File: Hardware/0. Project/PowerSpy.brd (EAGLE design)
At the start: 55 x 70.5 mm, 87 parts, among them CN1 Mini-Fit 4T, IC1 CP2102N-A01-GQFN28, T1 SS8050, T2 SS8050, U1 MCP6021, U2 MCP6024, U3 ADS1115IDGST, U4 HLK-PM01, U5 NCP1117ST33T3G, U6 ESP32-WROOM-32D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

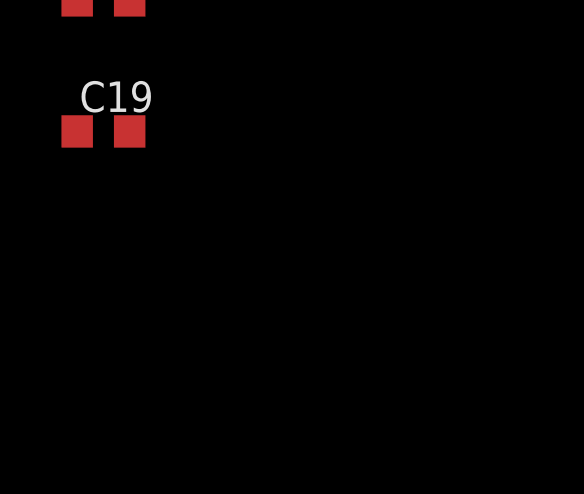
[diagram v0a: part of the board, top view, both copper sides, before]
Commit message: Pull-down resistor added to current AFE
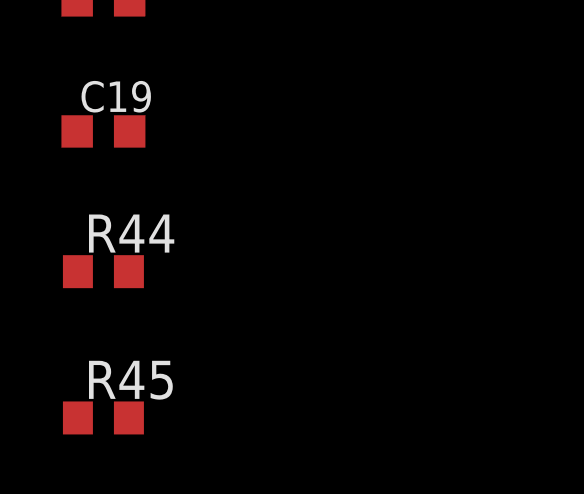
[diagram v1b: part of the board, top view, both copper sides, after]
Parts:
- added R44, R45: 1M (5%), rcl:R0603
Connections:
- net GND: now also R44.2, R45.2
- net N$35: now also R44.1
- net N$36: now also R45.1
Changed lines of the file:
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@@
 <attribute name="VALUE" x="-35.344" y="-184.1236" size="1.016" layer="27"/>
+</element>
+<element name="R44" library="rcl" library_urn="urn:adsk.eagle:library:334" package="R0603" package3d_urn="urn:adsk.eagle:package:23555/3" value="1M (5%)" x="-34.544" y="-187.1472" smashed="yes">
+<attribute name="NAME" x="-35.179" y="-186.5122" size="1.27" layer="25"/>
+<attribute name="POPULARITY" value="70" x="-34.544" y="-187.1472" size="1.778" layer="27" display="off"/>
+<attribute name="SPICEPREFIX" value="R" x="-34.544" y="-187.1472" size="1.778" layer="27" display="off"/>
+<attribute name="VALUE" x="-35.179" y="-189.0522" size="1.27" layer="27"/>
+</element>
+<element name="R45" library="rcl" library_urn="urn:adsk.eagle:library:334" package="R0603" package3d_urn="urn:adsk.eagle:package:23555/3" value="1M (5%)" x="-34.544" y="-192.024" smashed="yes">
+<attribute name="NAME" x="-35.179" y="-191.389" size="1.27" layer="25"/>
+<attribute name="POPULARITY" value="70" x="-34.544" y="-192.024" size="1.778" layer="27" display="off"/>
+<attribute name="SPICEPREFIX" value="R" x="-34.544" y="-192.024" size="1.778" layer="27" display="off"/>
+<attribute name="VALUE" x="-35.179" y="-193.929" size="1.27" layer="27"/>
 </element>
 </elements>
@@
 <contactref element="C3" pad="2"/>
 <contactref element="C19" pad="2"/>
+<contactref element="R44" pad="2"/>
+<contactref element="R45" pad="2"/>
+<wire x1="-33.694" y1="-187.1472" x2="-33.694" y2="-192.024" width="0" layer="19" extent="1-1"/>
+<wire x1="-33.669" y1="-182.4736" x2="-33.694" y2="-187.1472" width="0" layer="19" extent="1-1"/>
 <wire x1="-33.669" y1="-178.1048" x2="-33.669" y2="-182.4736" width="0" layer="19" extent="1-1"/>
 <wire x1="-35.3314" y1="-174.1424" x2="-33.669" y2="-178.1048" width="0" layer="19" extent="1-1"/>
@@
 <contactref element="U2" pad="10"/>
 <contactref element="X2" pad="1"/>
+<contactref element="R44" pad="1"/>
+<wire x1="-25.0786" y1="-115.062" x2="-35.394" y2="-187.1472" width="0" layer="19" extent="1-1"/>
 <wire x1="14" y1="10.345" x2="-25.0786" y2="-115.062" width="0" layer="19" extent="1-1"/>
 </signal>
@@
 <contactref element="X3" pad="1"/>
 <contactref element="U2" pad="12"/>
+<contactref element="R45" pad="1"/>
+<wire x1="-25.0786" y1="-112.522" x2="-35.394" y2="-192.024" width="0" layer="19" extent="1-1"/>
 <wire x1="14" y1="18.1" x2="-25.0786" y2="-112.522" width="0" layer="19" extent="1-1"/>
 </signal>

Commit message: ESP32 JLINK Pins added
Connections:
- new net JLINK-TCK: U6.16
- new net JLINK-TDI: U6.14
- new net JLINK-TDO: U6.23
- new net JLINK-TMS: U6.13
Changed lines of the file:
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@@
 <contactref element="X2" pad="2@1"/>
+</signal>
+<signal name="JLINK-TDO">
+<contactref element="U6" pad="23"/>
+</signal>
+<signal name="JLINK-TCK">
+<contactref element="U6" pad="16"/>
+</signal>
+<signal name="JLINK-TDI">
+<contactref element="U6" pad="14"/>
+</signal>
+<signal name="JLINK-TMS">
+<contactref element="U6" pad="13"/>
 </signal>
 </signals>
